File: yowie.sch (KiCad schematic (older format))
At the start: 16 parts

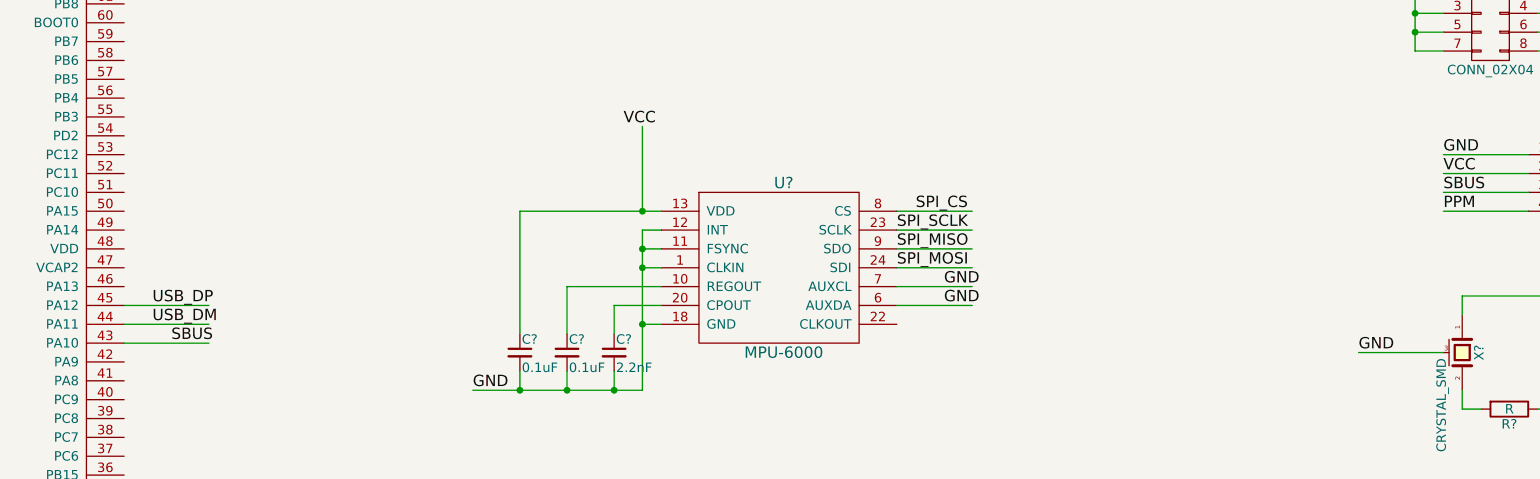
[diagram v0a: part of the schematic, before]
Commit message: Added SBUS Inverter
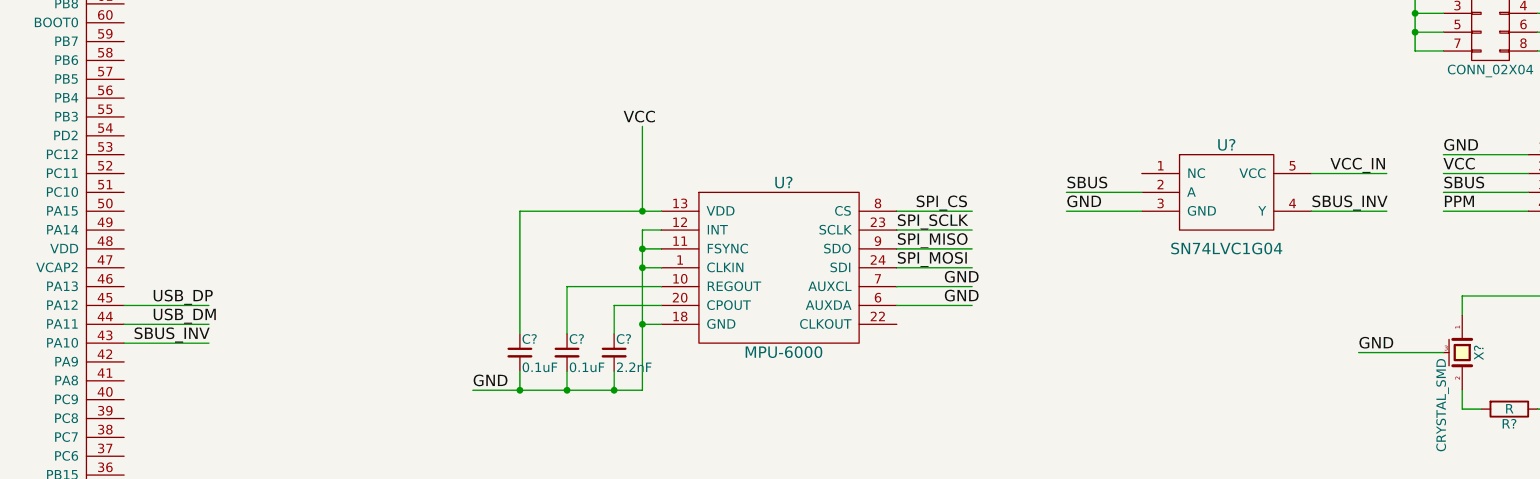
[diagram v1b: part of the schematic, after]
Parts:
- added U?: SN74LVC1G04, symbol SN74LVC1G04
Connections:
- net labels added: SBUS_INV
- wire segments 79 -> 83
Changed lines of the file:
@@
 Text Label 850  3550 0    60   ~ 0
 PPM
-Text Label 3400 2850 0    60   ~ 0
-SBUS
+Text Label 3200 2850 0    60   ~ 0
+SBUS_INV
 $Comp
 L CONN_02X04 P?
@@
 Text Label 850  2950 0    60   ~ 0
 SPI_MOSI
+$Comp
+L SN74LVC1G04 U?
+U 1 1 565D825E
+P 9000 1800
+F 0 "U?" H 9000 1800 60  0000 C CNN
+F 1 "SN74LVC1G04" H 9000 1250 60  0000 C CNN
+F 2 "" H 9000 1800 60  0000 C CNN
+F 3 "" H 9000 1800 60  0000 C CNN
+	1    9000 1800
+	1    0    0    -1
+$EndComp
+Wire Wire Line
+	9450 1950 9850 1950
+Wire Wire Line
+	9450 2150 9850 2150
+Wire Wire Line
+	8550 2150 8150 2150
+Wire Wire Line
+	8550 2050 8150 2050
+Text Label 9550 1950 0    60   ~ 0
+VCC_IN
+Text Label 9450 2150 0    60   ~ 0
+SBUS_INV
+Text Label 8150 2150 0    60   ~ 0
+GND
+Text Label 8150 2050 0    60   ~ 0
+SBUS
 $EndSCHEMATC

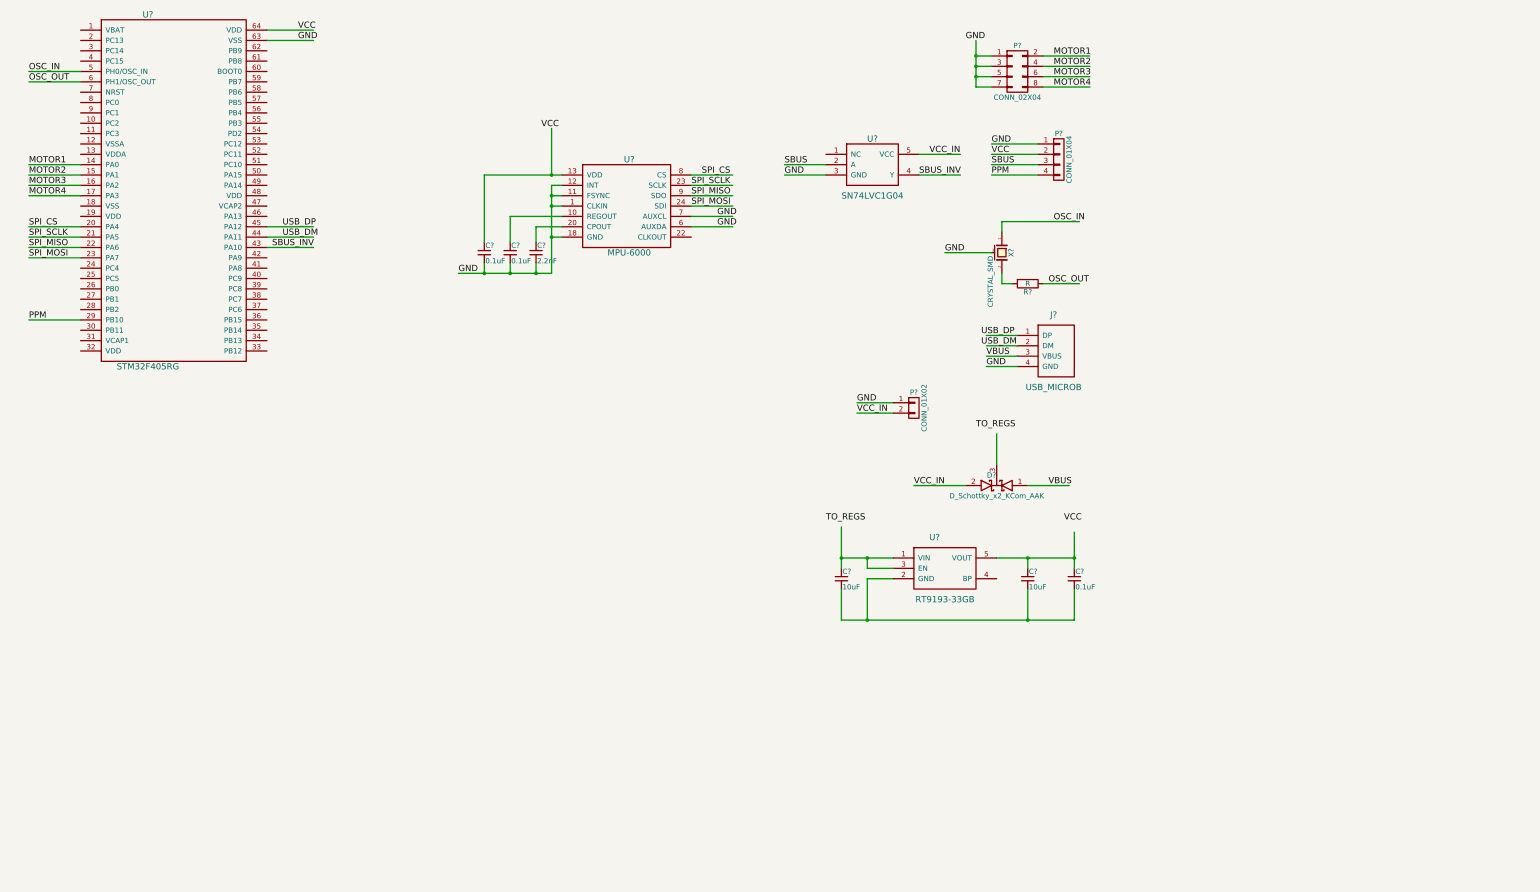
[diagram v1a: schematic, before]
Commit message: Added MAX7456
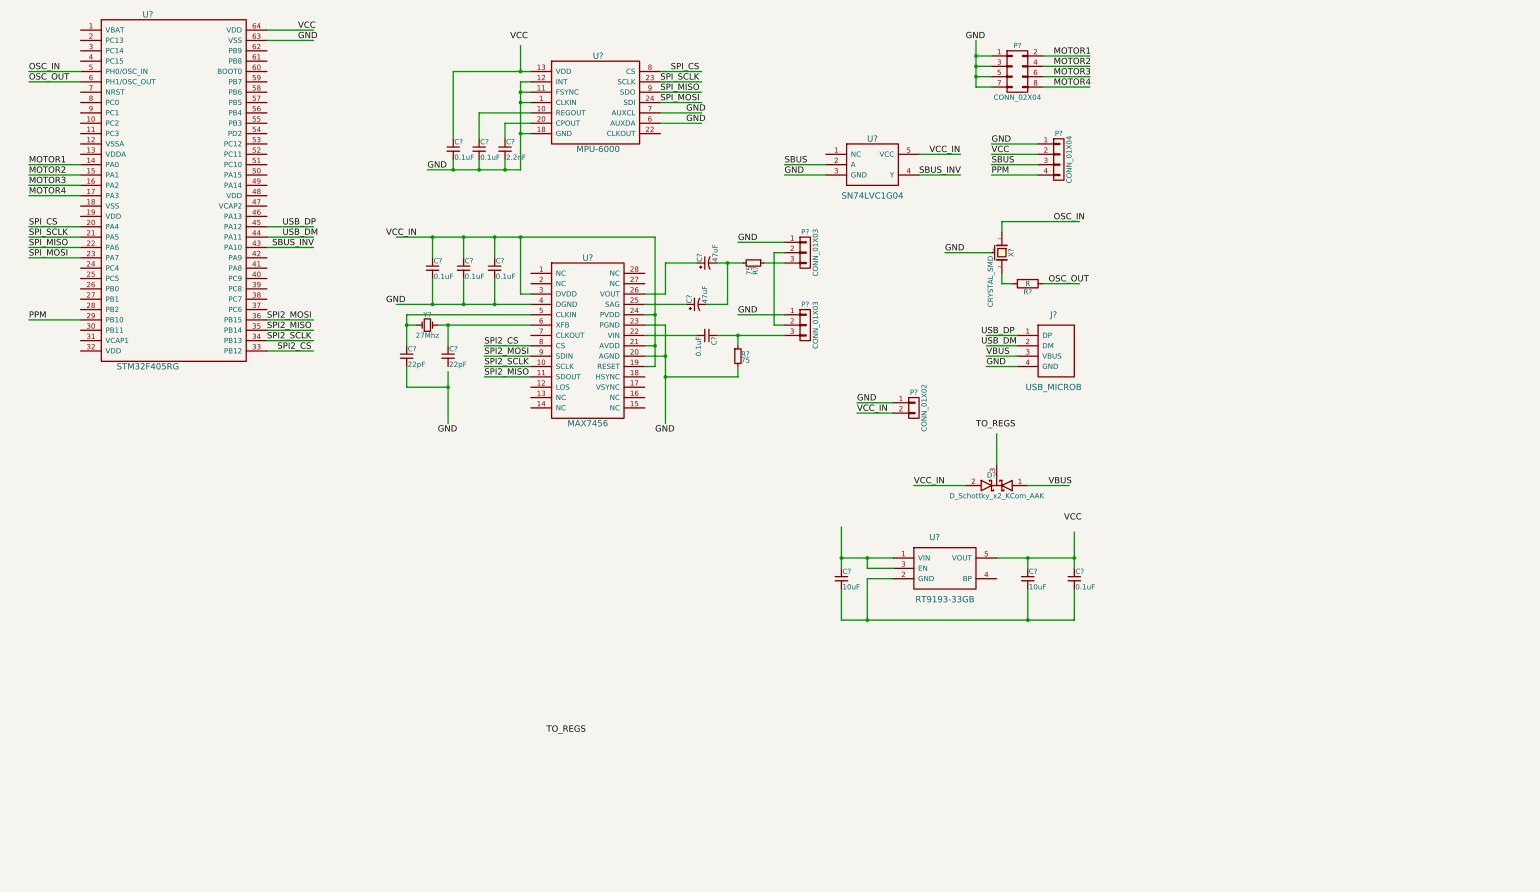
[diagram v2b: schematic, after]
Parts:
- added C? (x2): 22pF, symbol C_Small
- added C? (x4): 0.1uF, symbol C_Small
- added C? (x2): 47uF, symbol CP1_Small
- added P? (x2): CONN_01X03, symbol CONN_01X03
- added R? (x2): 75, symbol R_Small
- added U?: MAX7456, symbol MAX7456
- added Y?: 27Mhz, symbol Crystal_Small
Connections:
- net labels added: SPI2_CS, SPI2_MISO, SPI2_MOSI, SPI2_SCLK
- wire segments 83 -> 134
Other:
- moved on the sheet: C?, U?

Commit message: Added status LEDs, BUZZ out, VBAT in and RSSI in
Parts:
- added D? (x3): Led_Small, symbol Led_Small
- added P? (x3): CONN_01X02, symbol CONN_01X02
- added Q?: Q_PNP_BEC, symbol Q_PNP_BEC
- added R? (x3): 100, symbol R_Small
- added R? (x3): R_Small, symbol R_Small
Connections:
- net labels added: BUZZ, LED1, LED2, RSSI, VBAT
- wire segments 134 -> 160

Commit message: Added 3.3V and 5V regs and relabelled components to their required voltages
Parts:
- removed C? (x2): 10uF, symbol C_Small
- removed C?: 0.1uF, symbol C_Small
- removed U?: RT9193-33GB, symbol RT9193-33GB
- added C? (x4): 1uF, symbol C_Small
- added C? (x2): C_Small, symbol C_Small
- added L? (x2): L_Small, symbol L_Small
- added U? (x2): MAX15062, symbol MAX15062
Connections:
- net labels added: VCC_3_3V, VCC_5V
- net labels removed: VCC
- wire segments 160 -> 226
